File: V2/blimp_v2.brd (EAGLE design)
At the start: 62.3 x 57.1 mm, 10 parts

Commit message: upload the finished routing pcb design
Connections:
- net GND: no longer U$2.16, U$2.GND, U$4.16, U$4.GND
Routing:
- net GND: track 50.5 -> 145.8 mm
- net PWM1: track 17.4 -> 34.2 mm
- net PWM2: track 15.0 -> 31.2 mm
- net POWER: track 136.3 -> 143.2 mm
- net VCC: track 100.2 -> 102.6 mm
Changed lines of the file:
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@@
 <wire x1="91" y1="27" x2="82.41" y2="27" width="0.3048" layer="16"/>
 <wire x1="82.41" y1="27" x2="81.47" y2="27.94" width="0.3048" layer="16"/>
-<wire x1="81.47" y1="27.94" x2="83" y2="26.41" width="0.3048" layer="16"/>
-<wire x1="83" y1="6.61" x2="81.47" y2="5.08" width="0.3048" layer="16"/>
-<wire x1="83" y1="26.41" x2="83" y2="6.61" width="0.3048" layer="16"/>
+<wire x1="91" y1="27" x2="91" y2="6" width="0.3048" layer="16"/>
+<wire x1="91" y1="6" x2="90" y2="5" width="0.3048" layer="16"/>
+<wire x1="90" y1="5" x2="81.55" y2="5" width="0.3048" layer="16"/>
+<wire x1="81.55" y1="5" x2="81.47" y2="5.08" width="0.3048" layer="16"/>
 <wire x1="68" y1="52" x2="67.93" y2="50.23" width="0" layer="19" extent="16-16"/>
 </signal>
@@
 <contactref element="U$2" pad="6"/>
 <contactref element="JP4" pad="1"/>
-<contactref element="U$4" pad="16"/>
-<contactref element="U$4" pad="GND"/>
-<contactref element="U$2" pad="16"/>
-<contactref element="U$2" pad="GND"/>
 <polygon width="0.1524" layer="16">
 <vertex x="95.55" y="60.69"/>
@@
 <wire x1="51" y1="50" x2="51" y2="44.4937875" width="0.6096" layer="16"/>
 <wire x1="51" y1="44.4937875" x2="54.8" y2="40.6937875" width="0.6096" layer="16"/>
+<wire x1="76.39" y1="5.08" x2="76.235" y2="5.235" width="0.3048" layer="16"/>
+<wire x1="76.235" y1="5.235" x2="73.97" y2="7.5" width="0.3048" layer="16"/>
+<wire x1="73.97" y1="7.5" x2="61" y2="7.5" width="0.3048" layer="16"/>
+<wire x1="61" y1="7.5" x2="50.8" y2="7.5" width="0.3048" layer="16"/>
+<wire x1="50.8" y1="7.5" x2="50.8" y2="36.6937875" width="0.3048" layer="16"/>
+<wire x1="50.8" y1="36.6937875" x2="54.8" y2="40.6937875" width="0.3048" layer="16"/>
+<wire x1="76.5043125" y1="5.235" x2="76.235" y2="5.235" width="0.3048" layer="16"/>
+<wire x1="76.39" y1="27.94" x2="72.45" y2="24" width="0.3048" layer="16"/>
+<wire x1="72.45" y1="24" x2="61" y2="24" width="0.3048" layer="16"/>
+<wire x1="61" y1="24" x2="61" y2="7.5" width="0.3048" layer="16"/>
 <wire x1="65.93" y1="50.23" x2="66" y2="48" width="0" layer="19" extent="16-16"/>
-<wire x1="63.69" y1="43.18" x2="66" y2="48" width="0" layer="19" extent="16-16"/>
-<wire x1="63.69" y1="27.94" x2="63.69" y2="43.18" width="0" layer="19" extent="1-1"/>
-<wire x1="63.69" y1="20.32" x2="63.69" y2="27.94" width="0" layer="19" extent="1-1"/>
-<wire x1="76.39" y1="27.94" x2="63.69" y2="27.94" width="0" layer="19" extent="1-1"/>
-<wire x1="63.69" y1="5.08" x2="63.69" y2="20.32" width="0" layer="19" extent="1-1"/>
-<wire x1="76.39" y1="5.08" x2="63.69" y2="5.08" width="0" layer="19" extent="1-1"/>
 </signal>
 <signal name="VCC">
@@
 </polygon>
 <wire x1="55" y1="45.72" x2="54.8" y2="45.72" width="0.3048" layer="16"/>
-<wire x1="73.85" y1="43.18" x2="73.85" y2="42.15" width="0.3048" layer="16"/>
-<wire x1="78.93" y1="37.07" x2="78.93" y2="27.94" width="0.3048" layer="16"/>
-<wire x1="73.85" y1="42.15" x2="78.93" y2="37.07" width="0.3048" layer="16"/>
-<wire x1="78.93" y1="27.94" x2="73.85" y2="22.86" width="0.3048" layer="16"/>
-<wire x1="73.85" y1="22.86" x2="73.85" y2="20.32" width="0.3048" layer="16"/>
-<wire x1="73.85" y1="20.32" x2="73.85" y2="20.15" width="0.3048" layer="16"/>
-<wire x1="73.85" y1="20.15" x2="79" y2="15" width="0.3048" layer="16"/>
-<wire x1="79" y1="15" x2="79" y2="5.15" width="0.3048" layer="16"/>
+<wire x1="73.85" y1="20.15" x2="73.85" y2="20.32" width="0.3048" layer="16"/>
 <wire x1="79" y1="5.15" x2="78.93" y2="5.08" width="0.3048" layer="16"/>
 <contactref element="JP5" pad="2"/>
-<wire x1="54.8" y1="45.72" x2="71" y2="45.72" width="0.3048" layer="16"/>
-<wire x1="71" y1="45.72" x2="71.31" y2="45.72" width="0.3048" layer="16"/>
+<wire x1="54.8" y1="45.72" x2="71.31" y2="45.72" width="0.3048" layer="16"/>
 <wire x1="71.31" y1="45.72" x2="73.85" y2="43.18" width="0.3048" layer="16"/>
 <wire x1="79.15" y1="52.97" x2="87.47" y2="52.97" width="0.3048" layer="16"/>
@@
 <wire x1="90" y1="51" x2="90" y2="46" width="0.3048" layer="16"/>
 <wire x1="90" y1="46" x2="89.72" y2="45.72" width="0.3048" layer="16"/>
-<wire x1="89.72" y1="45.72" x2="71.31" y2="45.72" width="0.3048" layer="16"/>
+<wire x1="89.72" y1="45.72" x2="83" y2="45.72" width="0.3048" layer="16"/>
+<wire x1="83" y1="45.72" x2="71.31" y2="45.72" width="0.3048" layer="16"/>
+<wire x1="83" y1="45.72" x2="83" y2="32.01" width="0.3048" layer="16"/>
+<wire x1="83" y1="32.01" x2="78.93" y2="27.94" width="0.3048" layer="16"/>
+<wire x1="78.93" y1="27.94" x2="78.93" y2="25.4" width="0.3048" layer="16"/>
+<wire x1="78.93" y1="25.4" x2="73.85" y2="20.32" width="0.3048" layer="16"/>
+<wire x1="73.85" y1="20.32" x2="73.85" y2="10.16" width="0.3048" layer="16"/>
+<wire x1="73.85" y1="10.16" x2="78.93" y2="5.08" width="0.3048" layer="16"/>
 </signal>
 <signal name="N$1">
@@
 <contactref element="U$1" pad="19"/>
 <contactref element="U$4" pad="9"/>
+<wire x1="59.02" y1="33.02" x2="54.8" y2="33.02" width="0.3048" layer="16"/>
+<wire x1="66.23" y1="40.23" x2="66" y2="40" width="0.3048" layer="16"/>
+<wire x1="66" y1="40" x2="59.02" y2="33.02" width="0.3048" layer="16"/>
 <wire x1="66.23" y1="43.18" x2="66.23" y2="40.23" width="0.3048" layer="16"/>
-<wire x1="59.02" y1="33.02" x2="54.8" y2="33.02" width="0.3048" layer="16"/>
-<wire x1="66.23" y1="40.23" x2="59.02" y2="33.02" width="0.3048" layer="16"/>
-<wire x1="66.23" y1="43.18" x2="81.47" y2="43.18" width="0" layer="19" extent="1-1"/>
+<wire x1="66" y1="40" x2="78.29" y2="40" width="0.3048" layer="16"/>
+<wire x1="78.29" y1="40" x2="81.47" y2="43.18" width="0.3048" layer="16"/>
 </signal>
 <signal name="PWM2">
@@
 <contactref element="U$2" pad="9"/>
 <contactref element="U$2" pad="15"/>
-<wire x1="54.8" y1="25.4" x2="63.6" y2="25.4" width="0.3048" layer="16"/>
-<wire x1="66.23" y1="22.77" x2="66.23" y2="20.32" width="0.3048" layer="16"/>
-<wire x1="63.6" y1="25.4" x2="66.23" y2="22.77" width="0.3048" layer="16"/>
-<wire x1="66.23" y1="20.32" x2="81.47" y2="20.32" width="0" layer="19" extent="1-1"/>
+<wire x1="54.8" y1="25.4" x2="63.6" y2="25.4" width="0.3048" layer="1"/>
+<wire x1="66.23" y1="22.77" x2="63.6" y2="25.4" width="0.3048" layer="1"/>
+<wire x1="66.23" y1="20.32" x2="66.23" y2="22.77" width="0.3048" layer="1"/>
+<wire x1="66.23" y1="22.77" x2="79.02" y2="22.77" width="0.3048" layer="1"/>
+<wire x1="79.02" y1="22.77" x2="81.47" y2="20.32" width="0.3048" layer="1"/>
 </signal>
 <signal name="A3">

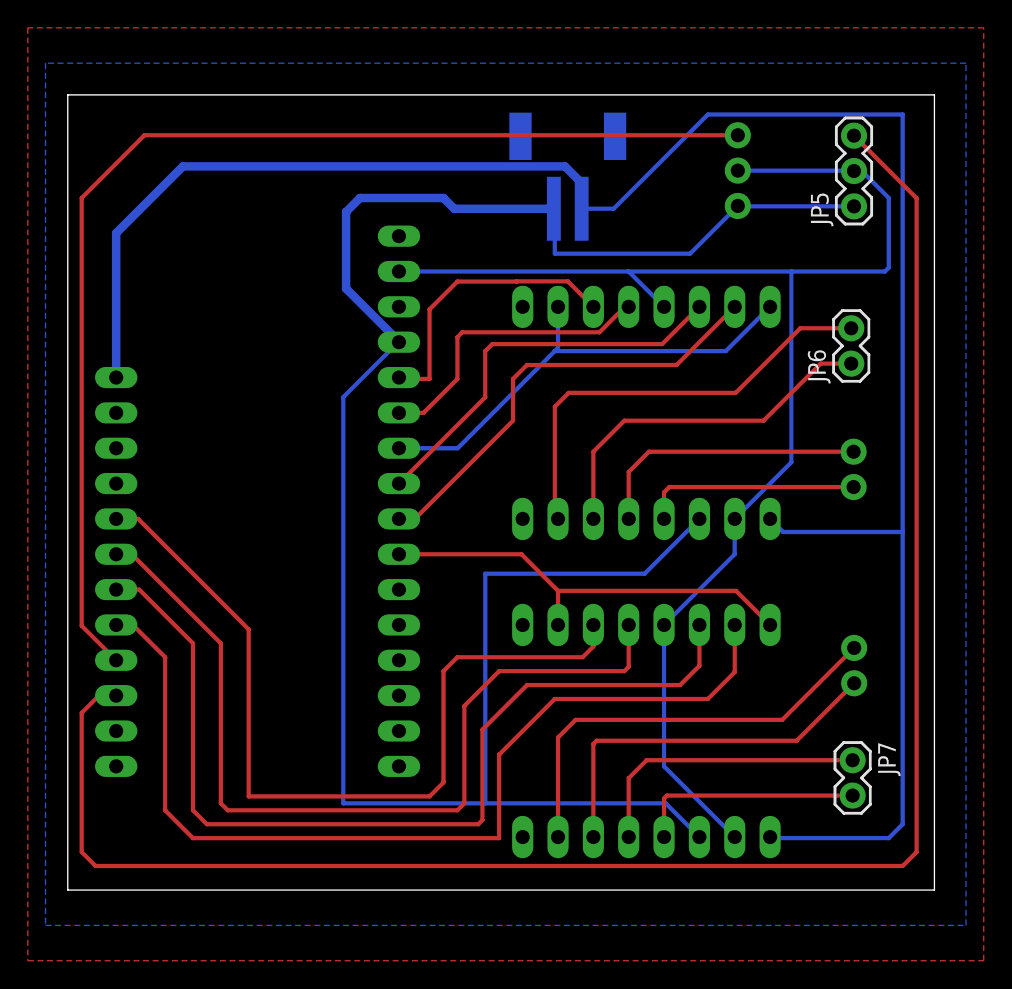
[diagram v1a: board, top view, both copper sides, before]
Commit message: add one more servo motor pinout
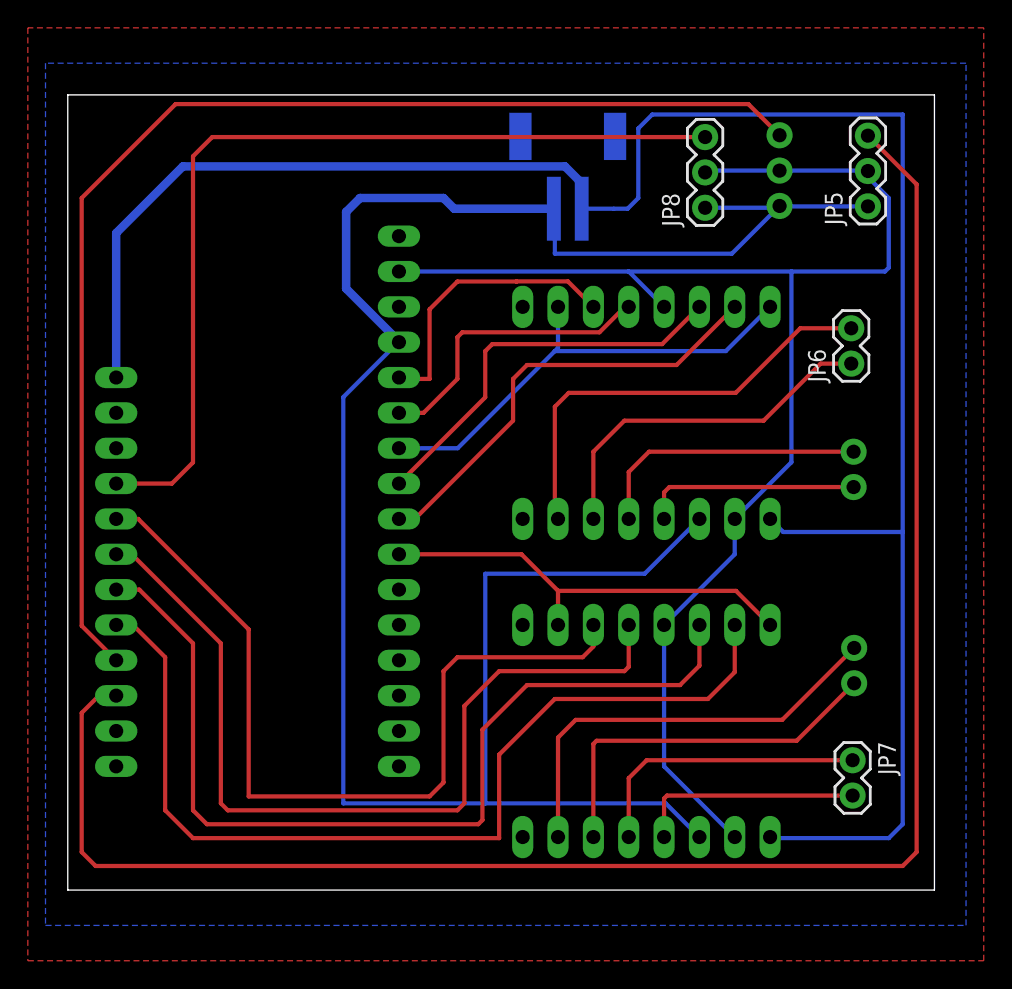
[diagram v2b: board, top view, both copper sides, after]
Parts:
- added JP8: (no value), SparkFun:1X03
- moved JP4 3.00 mm to (82.2, 50.4)
- moved JP5 1.00 mm to (88.5, 50.4)
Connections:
- net A12: now also JP8.3
- net GND: now also JP8.1
- net VCC: now also JP8.2
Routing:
- net A12: track 0.00 -> 65.5 mm
- net GND: track 145.8 -> 152.2 mm
- net D7: track 83.3 -> 88.1 mm
- net POWER: track 143.2 -> 146.1 mm
- net VCC: track 102.6 -> 105.2 mm
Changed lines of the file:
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@@
 <attribute name="VALUE" x="84.335" y="14.86" size="1.27" layer="28" rot="MR90"/>
 </element>
-<element name="JP4" library="SparkFun" package="1X03" value="" x="79.15" y="50.43" smashed="yes" rot="MR90">
-<attribute name="NAME" x="80.9788" y="49.0838" size="1.27" layer="26" ratio="10" rot="MR90"/>
-<attribute name="VALUE" x="75.975" y="49.16" size="1.27" layer="28" rot="MR90"/>
+<element name="JP4" library="SparkFun" package="1X03" value="" x="82.15" y="50.43" smashed="yes" rot="MR90">
+<attribute name="NAME" x="83.9788" y="49.0838" size="1.27" layer="26" ratio="10" rot="MR90"/>
+<attribute name="VALUE" x="78.975" y="49.16" size="1.27" layer="28" rot="MR90"/>
 </element>
 <element name="U$1" library="blimp" package="ESP32" value="ESP32" x="44.64" y="24.13" smashed="yes" rot="MR270">
@@
 <attribute name="VALUE" x="62.42" y="46.355" size="1.27" layer="28" rot="MR180"/>
 </element>
-<element name="JP5" library="SparkFun" package="1X03" value="" x="87.5" y="50.4" smashed="yes" rot="R90">
-<attribute name="NAME" x="85.6712" y="49.0538" size="1.27" layer="25" ratio="10" rot="R90"/>
-<attribute name="VALUE" x="90.675" y="49.13" size="1.27" layer="27" rot="R90"/>
+<element name="JP5" library="SparkFun" package="1X03" value="" x="88.5" y="50.4" smashed="yes" rot="R90">
+<attribute name="NAME" x="86.6712" y="49.0538" size="1.27" layer="25" ratio="10" rot="R90"/>
+<attribute name="VALUE" x="91.675" y="49.13" size="1.27" layer="27" rot="R90"/>
 </element>
 <element name="JP6" library="SparkFun" package="1X02" value="" x="87.3" y="39.1" smashed="yes" rot="R90">
@@
 <attribute name="NAME" x="89.2288" y="11.9462" size="1.27" layer="25" ratio="10" rot="R270"/>
 <attribute name="VALUE" x="84.225" y="11.87" size="1.27" layer="27" rot="R270"/>
+</element>
+<element name="JP8" library="SparkFun" package="1X03" value="" x="76.8" y="50.3" smashed="yes" rot="R90">
+<attribute name="NAME" x="74.9712" y="48.9538" size="1.27" layer="25" ratio="10" rot="R90"/>
+<attribute name="VALUE" x="79.975" y="49.03" size="1.27" layer="27" rot="R90"/>
 </element>
 </elements>
@@
 <wire x1="34.48" y1="48.48" x2="39.2728" y2="53.2728" width="0.6096" layer="16"/>
 <wire x1="39.2728" y1="53.2728" x2="66.7272" y2="53.2728" width="0.6096" layer="16"/>
-<wire x1="67.93" y1="50.23" x2="70.23" y2="50.23" width="0.3048" layer="16"/>
-<wire x1="70.23" y1="50.23" x2="77" y2="57" width="0.3048" layer="16"/>
-<wire x1="77" y1="57" x2="91" y2="57" width="0.3048" layer="16"/>
-<wire x1="91" y1="57" x2="91" y2="27" width="0.3048" layer="16"/>
+<wire x1="70.23" y1="50.23" x2="68" y2="50.23" width="0.3048" layer="16"/>
+<wire x1="68" y1="50.23" x2="67.93" y2="50.23" width="0.3048" layer="16"/>
+<wire x1="91" y1="27" x2="91" y2="57" width="0.3048" layer="16"/>
 <wire x1="91" y1="27" x2="82.41" y2="27" width="0.3048" layer="16"/>
 <wire x1="82.41" y1="27" x2="81.47" y2="27.94" width="0.3048" layer="16"/>
@@
 <wire x1="90" y1="5" x2="81.55" y2="5" width="0.3048" layer="16"/>
 <wire x1="81.55" y1="5" x2="81.47" y2="5.08" width="0.3048" layer="16"/>
+<wire x1="73" y1="57" x2="72" y2="56" width="0.3048" layer="16"/>
+<wire x1="72" y1="56" x2="72" y2="51" width="0.3048" layer="16"/>
+<wire x1="72" y1="51" x2="71.23" y2="50.23" width="0.3048" layer="16"/>
+<wire x1="71.23" y1="50.23" x2="70.23" y2="50.23" width="0.3048" layer="16"/>
+<wire x1="91" y1="57" x2="73" y2="57" width="0.3048" layer="16"/>
 <wire x1="68" y1="52" x2="67.93" y2="50.23" width="0" layer="19" extent="16-16"/>
 </signal>
@@
 <contactref element="JP5" pad="1"/>
 <wire x1="54.8" y1="40.6937875" x2="54.8" y2="40.64" width="0.6096" layer="16"/>
-<wire x1="79.15" y1="50.43" x2="75.72" y2="47" width="0.3048" layer="16"/>
-<wire x1="75.72" y1="47" x2="66" y2="47" width="0.3048" layer="16"/>
+<wire x1="82.15" y1="50.43" x2="78.72" y2="47" width="0.3048" layer="16"/>
+<wire x1="78.72" y1="47" x2="66" y2="47" width="0.3048" layer="16"/>
 <wire x1="66" y1="47" x2="66" y2="48" width="0.3048" layer="16"/>
-<wire x1="87.5" y1="50.4" x2="79.18" y2="50.4" width="0.3048" layer="16"/>
-<wire x1="79.18" y1="50.4" x2="79.15" y2="50.43" width="0.3048" layer="16"/>
+<wire x1="88.5" y1="50.4" x2="82.18" y2="50.4" width="0.3048" layer="16"/>
+<wire x1="82.18" y1="50.4" x2="82.15" y2="50.43" width="0.3048" layer="16"/>
 <wire x1="65.93" y1="50.23" x2="58.77" y2="50.23" width="0.6096" layer="16"/>
 <wire x1="58.77" y1="50.23" x2="58" y2="51" width="0.6096" layer="16"/>
@@
 <wire x1="72.45" y1="24" x2="61" y2="24" width="0.3048" layer="16"/>
 <wire x1="61" y1="24" x2="61" y2="7.5" width="0.3048" layer="16"/>
+<contactref element="JP8" pad="1"/>
+<wire x1="76.8" y1="50.3" x2="82.08" y2="50.3" width="0.3048" layer="16"/>
+<wire x1="82.08" y1="50.3" x2="82.18" y2="50.4" width="0.3048" layer="16"/>
 <wire x1="65.93" y1="50.23" x2="66" y2="48" width="0" layer="19" extent="16-16"/>
 </signal>
@@
 <wire x1="54.8" y1="45.72" x2="71.31" y2="45.72" width="0.3048" layer="16"/>
 <wire x1="71.31" y1="45.72" x2="73.85" y2="43.18" width="0.3048" layer="16"/>
-<wire x1="79.15" y1="52.97" x2="87.47" y2="52.97" width="0.3048" layer="16"/>
-<wire x1="87.47" y1="52.97" x2="87.5" y2="52.94" width="0.3048" layer="16"/>
-<wire x1="87.5" y1="52.94" x2="88.06" y2="52.94" width="0.3048" layer="16"/>
-<wire x1="88.06" y1="52.94" x2="90" y2="51" width="0.3048" layer="16"/>
+<wire x1="82.15" y1="52.97" x2="88.47" y2="52.97" width="0.3048" layer="16"/>
+<wire x1="88.47" y1="52.97" x2="88.5" y2="52.94" width="0.3048" layer="16"/>
+<wire x1="88.5" y1="52.94" x2="88.49999375" y2="52.50000625" width="0.3048" layer="16"/>
+<wire x1="88.49999375" y1="52.50000625" x2="90" y2="51" width="0.3048" layer="16"/>
 <wire x1="90" y1="51" x2="90" y2="46" width="0.3048" layer="16"/>
 <wire x1="90" y1="46" x2="89.72" y2="45.72" width="0.3048" layer="16"/>
@@
 <wire x1="73.85" y1="20.32" x2="73.85" y2="10.16" width="0.3048" layer="16"/>
 <wire x1="73.85" y1="10.16" x2="78.93" y2="5.08" width="0.3048" layer="16"/>
+<contactref element="JP8" pad="2"/>
+<wire x1="82.15" y1="52.97" x2="76.93" y2="52.97" width="0.3048" layer="16"/>
+<wire x1="76.93" y1="52.97" x2="76.8" y2="52.84" width="0.3048" layer="16"/>
 </signal>
 <signal name="N$1">
@@
 <contactref element="U$1" pad="9"/>
 <contactref element="JP4" pad="3"/>
-<wire x1="79.15" y1="55.51" x2="36.51" y2="55.51" width="0.3048" layer="1"/>
-<wire x1="36.51" y1="55.51" x2="32" y2="51" width="0.3048" layer="1"/>
-<wire x1="32" y1="51" x2="32" y2="20.26" width="0.3048" layer="1"/>
+<wire x1="32" y1="20.26" x2="32" y2="51" width="0.3048" layer="1"/>
 <wire x1="32" y1="20.26" x2="34.48" y2="17.78" width="0.3048" layer="1"/>
+<wire x1="80.66" y1="57" x2="80.83" y2="56.83" width="0.3048" layer="1"/>
+<wire x1="80.83" y1="56.83" x2="82.15" y2="55.51" width="0.3048" layer="1"/>
+<wire x1="79.9104" y1="57.7496" x2="80.66" y2="57" width="0.3048" layer="1"/>
+<wire x1="38.7496" y1="57.7496" x2="79.9104" y2="57.7496" width="0.3048" layer="1"/>
+<wire x1="32" y1="51" x2="38.7496" y2="57.7496" width="0.3048" layer="1"/>
 </signal>
 <signal name="D6">
 <contactref element="U$1" pad="10"/>
 <contactref element="JP5" pad="3"/>
-<wire x1="87.5" y1="55.48" x2="92" y2="50.98" width="0.3048" layer="1"/>
+<wire x1="88.5" y1="55.48" x2="92" y2="51.98" width="0.3048" layer="1"/>
 <wire x1="92" y1="4" x2="91" y2="3" width="0.3048" layer="1"/>
 <wire x1="91" y1="3" x2="33" y2="3" width="0.3048" layer="1"/>
@@
 <wire x1="32" y1="14" x2="33.24" y2="15.24" width="0.3048" layer="1"/>
 <wire x1="33.24" y1="15.24" x2="34.48" y2="15.24" width="0.3048" layer="1"/>
-<wire x1="92" y1="50.98" x2="92" y2="4" width="0.3048" layer="1"/>
+<wire x1="92" y1="51.98" x2="92" y2="4" width="0.3048" layer="1"/>
 </signal>
 <signal name="N$7">
@@
 <signal name="A12">
 <contactref element="U$1" pad="4"/>
+<contactref element="JP8" pad="3"/>
+<wire x1="76.8" y1="55.38" x2="41.38" y2="55.38" width="0.3048" layer="1"/>
+<wire x1="40" y1="54" x2="40" y2="32" width="0.3048" layer="1"/>
+<wire x1="40" y1="32" x2="38.48" y2="30.48" width="0.3048" layer="1"/>
+<wire x1="38.48" y1="30.48" x2="34.48" y2="30.48" width="0.3048" layer="1"/>
+<wire x1="41.38" y1="55.38" x2="40" y2="54" width="0.3048" layer="1"/>
 </signal>
 </signals>
